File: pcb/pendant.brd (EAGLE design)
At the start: 24 x 99 mm, 56 parts, among them CON1 USB_MICROSMT+THRUHULE, Q2 16MHz, SW2 BUTTON_2, T1 SSM3J328R,LF, T2 SSM3J328R,LF, U2 MK20D--VFM5, U3 74LVC1G17DCK, U4 74LVC1G17DCK

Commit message: Closing in on RevC design
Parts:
- moved D1 1.00 mm to (12.0, 72.0)
- moved D2 1.00 mm to (12.0, 78.0)
- moved D3 1.00 mm to (12.0, 84.0)
- moved D4 1.00 mm to (12.0, 90.0)
- moved D5 1.00 mm to (12.0, 96.0)
- moved CON1 0.50 mm to (2.10, 10.2)
- moved D10 0.50 mm to (12.0, 66.0)
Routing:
- net GND: track 8.53 -> 10.0 mm, vias 38 -> 37
- net R4: track 78.0 -> 79.0 mm
- net R3: track 72.1 -> 73.1 mm
- net R2: track 67.2 -> 68.2 mm
- net R1: track 67.8 -> 68.8 mm
- net R0: track 56.8 -> 57.8 mm
- net G4: track 76.7 -> 77.7 mm
- net G3: track 70.1 -> 71.1 mm
- net G1: track 64.9 -> 65.9 mm
- net G0: track 53.1 -> 54.1 mm
- net B4: track 76.1 -> 77.1 mm
- net B3: track 73.8 -> 74.8 mm
- net B2: track 65.8 -> 66.8 mm
- net B1: track 65.8 -> 66.8 mm
- net B0: track 46.1 -> 47.1 mm
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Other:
- board size 24 x 99 mm -> 24 x 100 mm
- board text added: "CLK"
- board text added: "DATA"
- board text added: "INT1"
- board text added: "OE"
- board text added: "OFF"
- board text added: "ON"
- board text added: "S0"
- board text added: "S1"
- board text added: "SCL"
- board text added: "SDA"
- board text added: "STB"

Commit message: RevC PCB
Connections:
- net GND: no longer U2.PAD@10, U2.PAD@2, U2.PAD@3, U2.PAD@5, U2.PAD@6
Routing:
- net GND: vias 37 -> 39
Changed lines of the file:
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@@
 <grid distance="0.5" unitdist="mm" unit="mm" style="lines" multiple="1" display="yes" altdistance="0.25" altunitdist="mm" altunit="mm"/>
 <layers>
-<layer number="1" name="Top" color="4" fill="1" visible="no" active="yes"/>
+<layer number="1" name="Top" color="4" fill="1" visible="yes" active="yes"/>
 <layer number="2" name="Route2" color="1" fill="3" visible="no" active="no"/>
 <layer number="3" name="Route3" color="4" fill="3" visible="no" active="no"/>
@@
 <layer number="19" name="Unrouted" color="6" fill="1" visible="yes" active="yes"/>
 <layer number="20" name="Dimension" color="15" fill="1" visible="yes" active="yes"/>
-<layer number="21" name="tPlace" color="6" fill="1" visible="no" active="yes"/>
+<layer number="21" name="tPlace" color="6" fill="1" visible="yes" active="yes"/>
 <layer number="22" name="bPlace" color="3" fill="1" visible="yes" active="yes"/>
 <layer number="23" name="tOrigins" color="15" fill="1" visible="yes" active="yes"/>
 <layer number="24" name="bOrigins" color="15" fill="1" visible="yes" active="yes"/>
-<layer number="25" name="tNames" color="7" fill="1" visible="yes" active="yes"/>
+<layer number="25" name="tNames" color="7" fill="1" visible="no" active="yes"/>
 <layer number="26" name="bNames" color="7" fill="1" visible="no" active="yes"/>
 <layer number="27" name="tValues" color="7" fill="1" visible="no" active="yes"/>
 <layer number="28" name="bValues" color="7" fill="1" visible="no" active="yes"/>
-<layer number="29" name="tStop" color="7" fill="3" visible="no" active="yes"/>
-<layer number="30" name="bStop" color="7" fill="6" visible="no" active="yes"/>
-<layer number="31" name="tCream" color="13" fill="4" visible="no" active="yes"/>
-<layer number="32" name="bCream" color="7" fill="5" visible="no" active="yes"/>
-<layer number="33" name="tFinish" color="6" fill="3" visible="no" active="yes"/>
-<layer number="34" name="bFinish" color="6" fill="6" visible="no" active="yes"/>
-<layer number="35" name="tGlue" color="7" fill="4" visible="no" active="yes"/>
-<layer number="36" name="bGlue" color="7" fill="5" visible="no" active="yes"/>
-<layer number="37" name="tTest" color="7" fill="1" visible="no" active="yes"/>
-<layer number="38" name="bTest" color="7" fill="1" visible="no" active="yes"/>
+<layer number="29" name="tStop" color="7" fill="3" visible="yes" active="yes"/>
+<layer number="30" name="bStop" color="7" fill="6" visible="yes" active="yes"/>
+<layer number="31" name="tCream" color="13" fill="4" visible="yes" active="yes"/>
+<layer number="32" name="bCream" color="7" fill="5" visible="yes" active="yes"/>
+<layer number="33" name="tFinish" color="6" fill="3" visible="yes" active="yes"/>
+<layer number="34" name="bFinish" color="6" fill="6" visible="yes" active="yes"/>
+<layer number="35" name="tGlue" color="7" fill="4" visible="yes" active="yes"/>
+<layer number="36" name="bGlue" color="7" fill="5" visible="yes" active="yes"/>
+<layer number="37" name="tTest" color="7" fill="1" visible="yes" active="yes"/>
+<layer number="38" name="bTest" color="7" fill="1" visible="yes" active="yes"/>
 <layer number="39" name="tKeepout" color="4" fill="11" visible="no" active="yes"/>
 <layer number="40" name="bKeepout" color="1" fill="11" visible="no" active="yes"/>
@@
 <contactref element="Q2" pad="P$2"/>
 <contactref element="Q2" pad="P$4"/>
-<contactref element="U2" pad="PAD@10"/>
 <contactref element="U2" pad="2"/>
-<contactref element="U2" pad="PAD@6"/>
-<contactref element="U2" pad="PAD@3"/>
 <contactref element="U2" pad="PAD@9"/>
-<contactref element="U2" pad="PAD@2"/>
 <contactref element="U2" pad="PAD@4"/>
 <contactref element="U2" pad="PAD@1"/>
 <contactref element="U2" pad="PAD@11"/>
-<contactref element="U2" pad="PAD@5"/>
 <contactref element="U2" pad="8"/>
 <contactref element="C17" pad="2"/>
@@
 <via x="18" y="6.5" extent="1-16" drill="0.35"/>
 <via x="21.75" y="4.5" extent="1-16" drill="0.35"/>
-<contactref element="SW2" pad="SHEILD_2"/>
-<contactref element="SW2" pad="SHEILD_3"/>
-<contactref element="SW2" pad="SHEILD_4"/>
 <wire x1="22.725" y1="22.75" x2="22.725" y2="23.075" width="0.4064" layer="1"/>
 <wire x1="22.725" y1="23.075" x2="22.4" y2="23.4" width="0.4064" layer="1"/>
@@
 <wire x1="10.95" y1="23.4" x2="10.35" y2="23.4" width="0.254" layer="1"/>
 <wire x1="10.35" y1="23.4" x2="10" y2="23.75" width="0.254" layer="1"/>
+<via x="10.25" y="36.25" extent="1-16" drill="0.35"/>
+<via x="12.25" y="74.75" extent="1-16" drill="0.35"/>
+<contactref element="SW2" pad="SHEILD_2"/>
+<contactref element="SW2" pad="SHEILD_3"/>
+<contactref element="SW2" pad="SHEILD_4"/>
 </signal>
 <signal name="LED_OE">

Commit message: Update board
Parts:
- added TP18, TP19, TP20, TP21, TP22, TP23, TP24, TP25, TP26, TP27, TP28, TP29, TP30, TP31, TP32, TP33, TP34: PTR1B1,27, testpad:B1,27
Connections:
- removed net USB_SHIELD: CON1.PAD$1, CON1.PAD$10, CON1.PAD$2, CON1.PAD$3, CON1.PAD$4, CON1.PAD$5, CON1.PAD$6, CON1.PAD$7, CON1.PAD$8, CON1.PAD$9
- net B0: now also TP20.TP
- net B1: now also TP23.TP
- net B2: now also TP25.TP
- net B3: now also TP29.TP
- net B4: now also TP32.TP
- net G0: now also TP19.TP
- net G1: now also TP22.TP
- net G2: now also TP26.TP
- net G3: now also TP28.TP
- net G4: now also TP31.TP
- net GND: now also CON1.PAD$1, CON1.PAD$10, CON1.PAD$2, CON1.PAD$3, CON1.PAD$4, CON1.PAD$5, CON1.PAD$6, CON1.PAD$7, CON1.PAD$8, CON1.PAD$9
- net R0: now also TP18.TP
- net R1: now also TP21.TP
- net R2: now also TP24.TP
- net R3: now also TP27.TP
- net R4: now also TP30.TP
- net S0: now also TP33.TP
- net S1: now also TP34.TP
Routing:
- net G4: track 77.7 -> 80.1 mm
- net G3: track 71.1 -> 73.5 mm
- net B0: track 47.1 -> 49.4 mm, vias 0 -> 1
- net G0: track 54.1 -> 56.2 mm
- net R4: track 79.0 -> 81.0 mm
- net R3: track 73.1 -> 75.1 mm
- net R0: track 57.8 -> 59.8 mm
- net B3: track 74.8 -> 76.8 mm
- net B2: track 66.8 -> 68.8 mm
- net B4: track 77.1 -> 78.1 mm
- net G1: track 65.9 -> 66.5 mm
- net S1: vias 0 -> 1
- net S0: vias 2 -> 3
- net GND: vias 39 -> 40
- removed copper zone on layer 1, net USB_SHIELD
- removed copper zone on layer 16, net USB_SHIELD
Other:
- board text added: "PENDANT Rev D 2015-05-05 blinkinlabs.com"

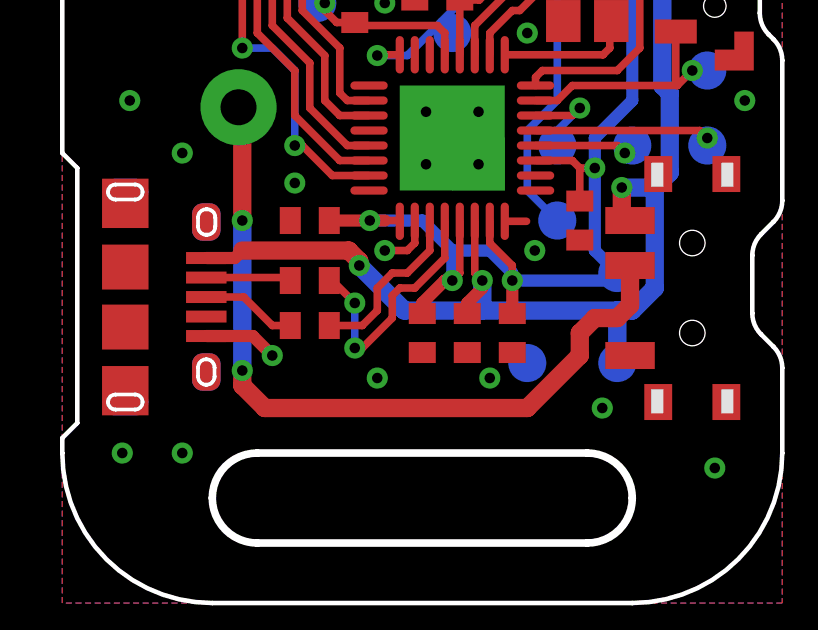
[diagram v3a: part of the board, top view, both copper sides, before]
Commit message: Add USB, VBAT test points
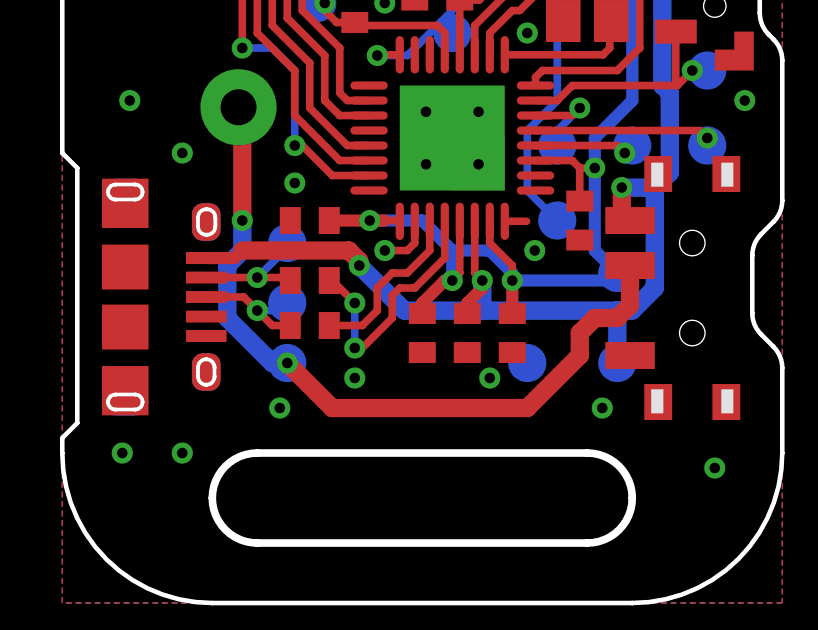
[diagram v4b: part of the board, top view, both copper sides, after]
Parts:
- added TP35, TP36, TP37: PTR1B1,27, testpad:B1,27
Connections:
- removed net N$2: U$1.+, U$2.COM
- new net VBAT: TP37.TP, U$1.+, U$2.COM
- net N$14: now also TP36.TP
- net N$21: now also TP35.TP
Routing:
- net N$2: track 25.7 -> 0.00 mm, vias 2 -> 0
- net VBAT: track 0.00 -> 25.1 mm, vias 0 -> 2
- net GND: track 10.0 -> 7.53 mm
- net N$21: track 2.84 -> 4.41 mm, vias 0 -> 1
- net N$14: track 3.19 -> 4.30 mm, vias 0 -> 1
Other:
- board text added: "5V"
- board text added: "D+"
- board text added: "D-"
- board text added: "VUSB"
- board text removed: "VBAT"
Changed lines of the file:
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@@
 <setting verticaltext="up"/>
 </settings>
-<grid distance="5" unitdist="mm" unit="mm" style="lines" multiple="1" display="yes" altdistance="2.5" altunitdist="mm" altunit="mm"/>
+<grid distance="1" unitdist="mm" unit="mm" style="lines" multiple="1" display="yes" altdistance="0.25" altunitdist="mm" altunit="mm"/>
 <layers>
 <layer number="1" name="Top" color="4" fill="1" visible="yes" active="yes"/>
@@
 <layer number="17" name="Pads" color="2" fill="1" visible="yes" active="yes"/>
 <layer number="18" name="Vias" color="2" fill="1" visible="yes" active="yes"/>
-<layer number="19" name="Unrouted" color="6" fill="1" visible="no" active="yes"/>
+<layer number="19" name="Unrouted" color="6" fill="1" visible="yes" active="yes"/>
 <layer number="20" name="Dimension" color="15" fill="1" visible="yes" active="yes"/>
 <layer number="21" name="tPlace" color="6" fill="1" visible="no" active="yes"/>
-<layer number="22" name="bPlace" color="3" fill="1" visible="no" active="yes"/>
-<layer number="23" name="tOrigins" color="15" fill="1" visible="no" active="yes"/>
-<layer number="24" name="bOrigins" color="15" fill="1" visible="no" active="yes"/>
+<layer number="22" name="bPlace" color="3" fill="1" visible="yes" active="yes"/>
+<layer number="23" name="tOrigins" color="15" fill="1" visible="yes" active="yes"/>
+<layer number="24" name="bOrigins" color="15" fill="1" visible="yes" active="yes"/>
 <layer number="25" name="tNames" color="7" fill="1" visible="no" active="yes"/>
 <layer number="26" name="bNames" color="7" fill="1" visible="no" active="yes"/>
@@
 <layer number="44" name="Drills" color="7" fill="1" visible="no" active="yes"/>
 <layer number="45" name="Holes" color="7" fill="1" visible="no" active="yes"/>
-<layer number="46" name="Milling" color="3" fill="1" visible="no" active="yes"/>
+<layer number="46" name="Milling" color="3" fill="1" visible="yes" active="yes"/>
 <layer number="47" name="Measures" color="7" fill="1" visible="no" active="yes"/>
 <layer number="48" name="Document" color="7" fill="1" visible="no" active="yes"/>
@@
 <text x="16.25" y="16.5" size="0.635" layer="22" font="vector" ratio="20" rot="MR0" align="center">TX</text>
 <text x="18.5" y="12.25" size="0.635" layer="22" font="vector" ratio="20" rot="MR0" align="center">3.3V</text>
-<text x="18.5" y="9" size="0.635" layer="22" font="vector" ratio="20" rot="MR180" align="center">VBAT</text>
+<text x="18.5" y="9" size="0.635" layer="22" font="vector" ratio="20" rot="MR180" align="center">5V</text>
 <wire x1="5" y1="3.5" x2="6.5" y2="2" width="0.254" layer="20" curve="90"/>
 <wire x1="6.5" y1="2" x2="17.5" y2="2" width="0.254" layer="20"/>
@@
 <wire x1="12.5" y1="100" x2="22.5" y2="100" width="0.254" layer="209"/>
 <wire x1="22.5" y1="100" x2="22.5" y2="40" width="0.254" layer="209"/>
+<text x="7.5" y="13" size="0.635" layer="22" font="vector" ratio="20" rot="MR0" align="center">D-</text>
+<text x="7.5" y="11" size="0.635" layer="22" font="vector" ratio="20" rot="MR0" align="center">D+</text>
+<text x="7.5" y="9" size="0.635" layer="22" font="vector" ratio="20" rot="MR0" align="center">VUSB</text>
 </plain>
 <attributes>
@@
 <attribute name="TP_SIGNAL_NAME" value="" x="16" y="43" size="1.016" layer="28" font="vector" rot="MR0" display="off"/>
 </element>
+<element name="TP35" library="testpad" package="B1,27" value="PTR1B1,27" x="7.5" y="12" rot="MR0">
+<attribute name="TP_SIGNAL_NAME" value="" x="7.5" y="12" size="0.04571875" layer="28" font="vector" rot="MR0" display="off"/>
+</element>
+<element name="TP36" library="testpad" package="B1,27" value="PTR1B1,27" x="7.5" y="10" rot="MR0">
+<attribute name="TP_SIGNAL_NAME" value="" x="7.5" y="10" size="0.04571875" layer="28" font="vector" rot="MR0" display="off"/>
+</element>
+<element name="TP37" library="testpad" package="B1,27" value="PTR1B1,27" x="7.5" y="8" rot="MR0">
+<attribute name="TP_SIGNAL_NAME" value="" x="7.5" y="8" size="0.04571875" layer="28" font="vector" rot="MR0" display="off"/>
+</element>
 </elements>
 <signals>
@@
 <wire x1="10.95" y1="22.6" x2="10.1" y2="22.6" width="0.254" layer="1"/>
 <wire x1="10.1" y1="22.6" x2="9.75" y2="22.25" width="0.254" layer="1"/>
-<via x="7" y="8.25" extent="1-16" drill="0.35"/>
+<via x="7.25" y="6.5" extent="1-16" drill="0.35"/>
 <via x="4" y="5" extent="1-16" drill="0.35"/>
 <via x="22.25" y="24.75" extent="1-16" drill="0.35"/>
@@
 <via x="22.5" y="65.25" extent="1-16" drill="0.35"/>
 <via x="22.25" y="51.25" extent="1-16" drill="0.35"/>
-<via x="10.5" y="7.5" extent="1-16" drill="0.35"/>
+<via x="9.75" y="7.5" extent="1-16" drill="0.35"/>
 <contactref element="SW2" pad="SHEILD_1"/>
 <via x="7.75" y="14" extent="1-16" drill="0.35"/>
@@
 <wire x1="22.725" y1="18.425" x2="22.4" y2="18.1" width="0.4064" layer="1"/>
 <contactref element="SW2" pad="1"/>
-<wire x1="4.8" y1="8.9" x2="6.35" y2="8.9" width="0.4064" layer="1"/>
-<wire x1="6.35" y1="8.9" x2="7" y2="8.25" width="0.4064" layer="1"/>
 <wire x1="10.95" y1="23.8" x2="10.05" y2="23.8" width="0.254" layer="1"/>
 <wire x1="10.05" y1="23.8" x2="10" y2="23.75" width="0.254" layer="1"/>
@@
 <contactref element="CON1" pad="PIN$3"/>
 <wire x1="4.8" y1="10.2" x2="6.05" y2="10.2" width="0.254" layer="1"/>
-<wire x1="6.05" y1="10.2" x2="7" y2="9.25" width="0.254" layer="1"/>
 <wire x1="7.6" y1="9.25" x2="7" y2="9.25" width="0.254" layer="1"/>
+<wire x1="7" y1="9.25" x2="6.5" y2="9.75" width="0.254" layer="1"/>
+<contactref element="TP36" pad="TP"/>
+<wire x1="7.5" y1="10" x2="7.25" y2="9.75" width="0.254" layer="16"/>
+<wire x1="7.25" y1="9.75" x2="6.5" y2="9.75" width="0.254" layer="16"/>
+<via x="6.5" y="9.75" extent="1-16" drill="0.35"/>
+<wire x1="6.5" y1="9.75" x2="6.05" y2="10.2" width="0.254" layer="1"/>
 </signal>
 <signal name="N$15">
@@
 <contactref element="R6" pad="1"/>
 <contactref element="CON1" pad="PIN$2"/>
-<wire x1="4.8" y1="10.85" x2="7.5" y2="10.85" width="0.254" layer="1"/>
+<wire x1="4.8" y1="10.85" x2="6.5" y2="10.85" width="0.254" layer="1"/>
 <wire x1="7.5" y1="10.85" x2="7.6" y2="10.75" width="0.254" layer="1"/>
+<contactref element="TP35" pad="TP"/>
+<via x="6.5" y="10.85" extent="1-16" drill="0.35"/>
+<wire x1="6.5" y1="10.85" x2="7.5" y2="10.85" width="0.254" layer="1"/>
+<wire x1="7.5" y1="12" x2="7.5" y2="11.85" width="0.254" layer="16"/>
+<wire x1="7.5" y1="11.85" x2="6.5" y2="10.85" width="0.254" layer="16"/>
 </signal>
 <signal name="LED_DATA">
@@
 <contactref element="TP30" pad="TP"/>
 </signal>
-<signal name="N$2">
+<signal name="VBAT">
 <contactref element="U$1" pad="+"/>
 <wire x1="5.875" y1="16.5251625" x2="6" y2="16.4001625" width="0.6096" layer="1"/>
 <wire x1="6" y1="16.4001625" x2="6" y2="12.75" width="0.6096" layer="1"/>
 <via x="6" y="12.75" extent="1-16" drill="0.35"/>
-<wire x1="6" y1="12.75" x2="6" y2="7.75" width="0.6096" layer="16"/>
-<via x="6" y="7.75" extent="1-16" drill="0.35"/>
-<wire x1="6" y1="7.75" x2="6" y2="7.25" width="0.6096" layer="1"/>
-<wire x1="6" y1="7.25" x2="6.75" y2="6.5" width="0.6096" layer="1"/>
-<wire x1="6.75" y1="6.5" x2="15.5" y2="6.5" width="0.6096" layer="1"/>
+<wire x1="6" y1="12.75" x2="6" y2="11.75" width="0.6096" layer="16"/>
+<wire x1="6" y1="11.75" x2="5.5" y2="11.25" width="0.6096" layer="16"/>
+<wire x1="5.5" y1="11.25" x2="5.5" y2="9.5" width="0.6096" layer="16"/>
+<wire x1="5.5" y1="9.5" x2="7" y2="8" width="0.6096" layer="16"/>
+<wire x1="7" y1="8" x2="7.5" y2="8" width="0.6096" layer="16"/>
+<via x="7.5" y="8" extent="1-16" drill="0.35"/>
+<wire x1="7.5" y1="8" x2="9" y2="6.5" width="0.6096" layer="1"/>
+<wire x1="9" y1="6.5" x2="15.5" y2="6.5" width="0.6096" layer="1"/>
 <wire x1="15.5" y1="6.5" x2="17.25" y2="8.25" width="0.6096" layer="1"/>
 <contactref element="U$2" pad="COM"/>
@@
 <wire x1="17.75" y1="9.5" x2="17.25" y2="9" width="0.6096" layer="1"/>
 <wire x1="17.25" y1="9" x2="17.25" y2="8.25" width="0.6096" layer="1"/>
+<contactref element="TP37" pad="TP"/>
 </signal>
 </signals>
